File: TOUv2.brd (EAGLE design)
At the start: 30.1 x 27.9 mm, 9 parts, among them Q1 32.768KHz, U1 ATTINY85-20SU, U3 LIGHTSENSORALS

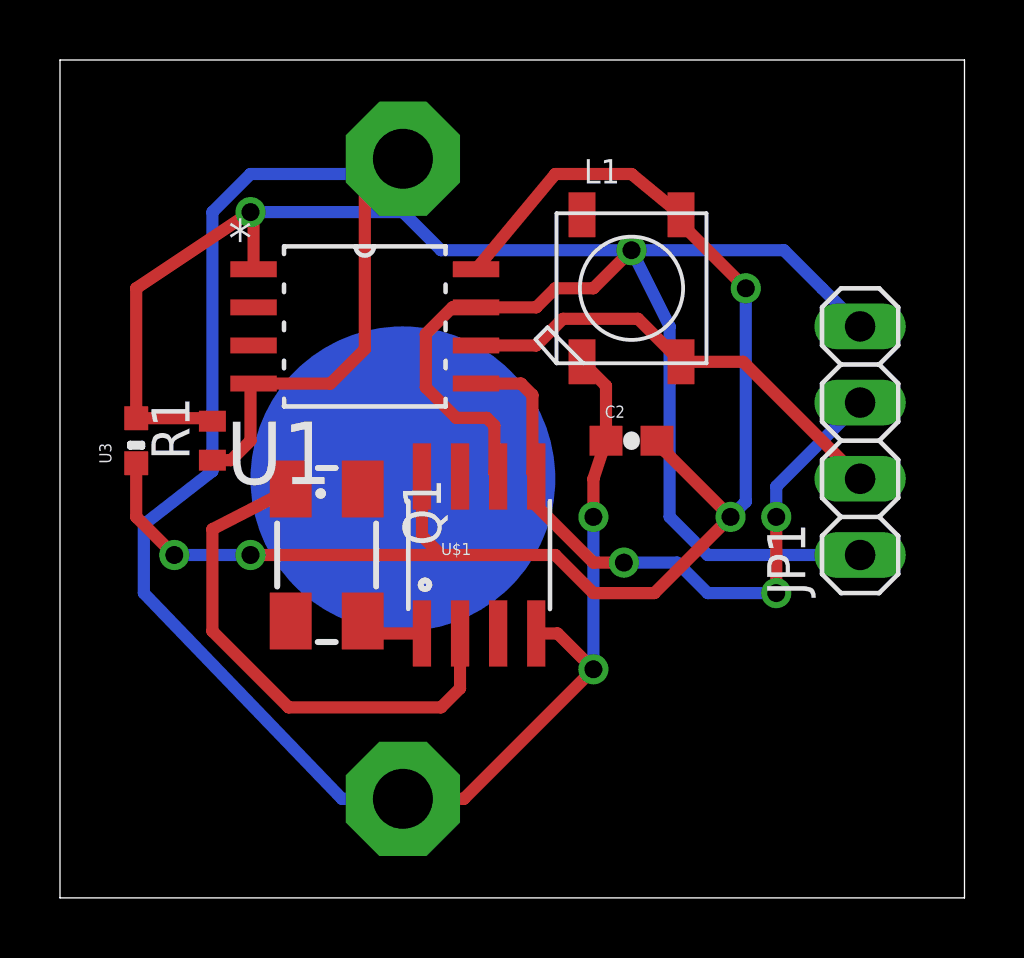
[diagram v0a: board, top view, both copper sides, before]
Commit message: Fix CR2032 error, simplify routing, add BOM
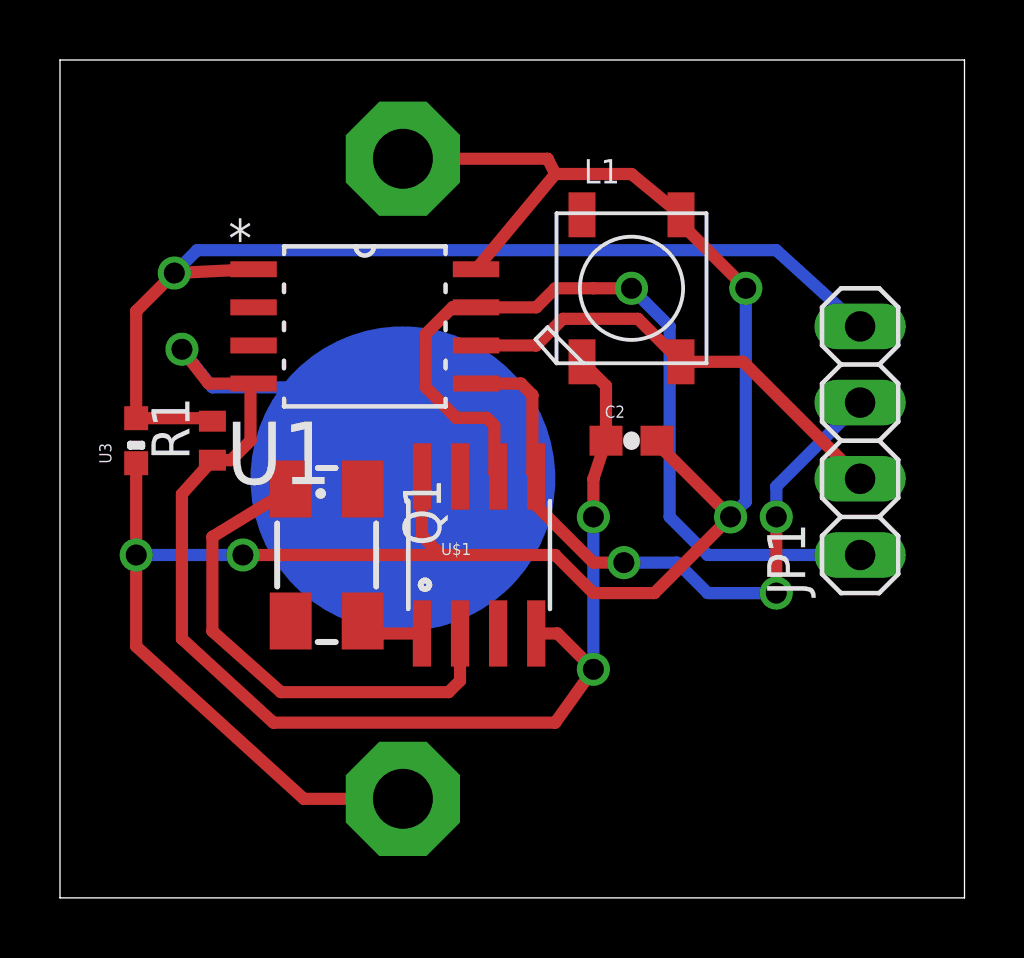
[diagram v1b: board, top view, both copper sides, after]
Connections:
- net GND: now also B1.-; no longer B1.+1, B1.+2
- net VCC: now also B1.+1, B1.+2; no longer B1.-
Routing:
- net GND: track 68.4 -> 50.7 mm, vias 2 -> 3
- net VCC: track 54.1 -> 70.1 mm
- net SCL/SCK: track 30.5 -> 29.0 mm
- net N$1: track 17.7 -> 17.0 mm
- net LDR/RST: track 35.3 -> 34.7 mm
